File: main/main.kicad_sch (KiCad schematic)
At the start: 8 parts, among them J1 USB_C_Receptacle_USB2.0, U1 ATmega32U4-A, Y1 16MHz

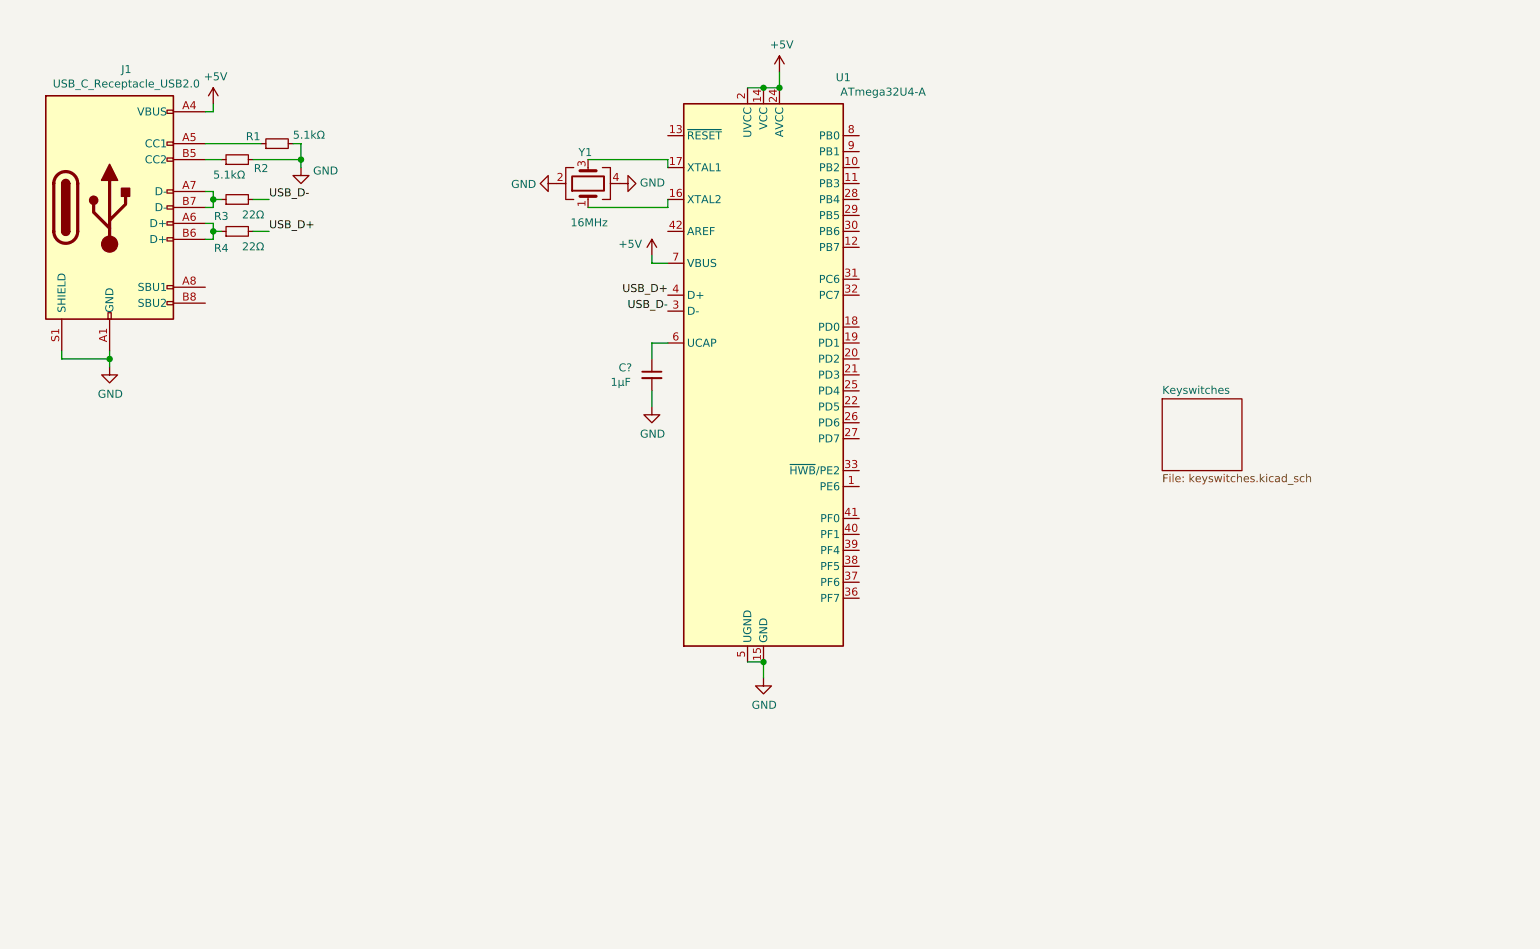
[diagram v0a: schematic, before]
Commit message: Add proposed layout, start LEDs
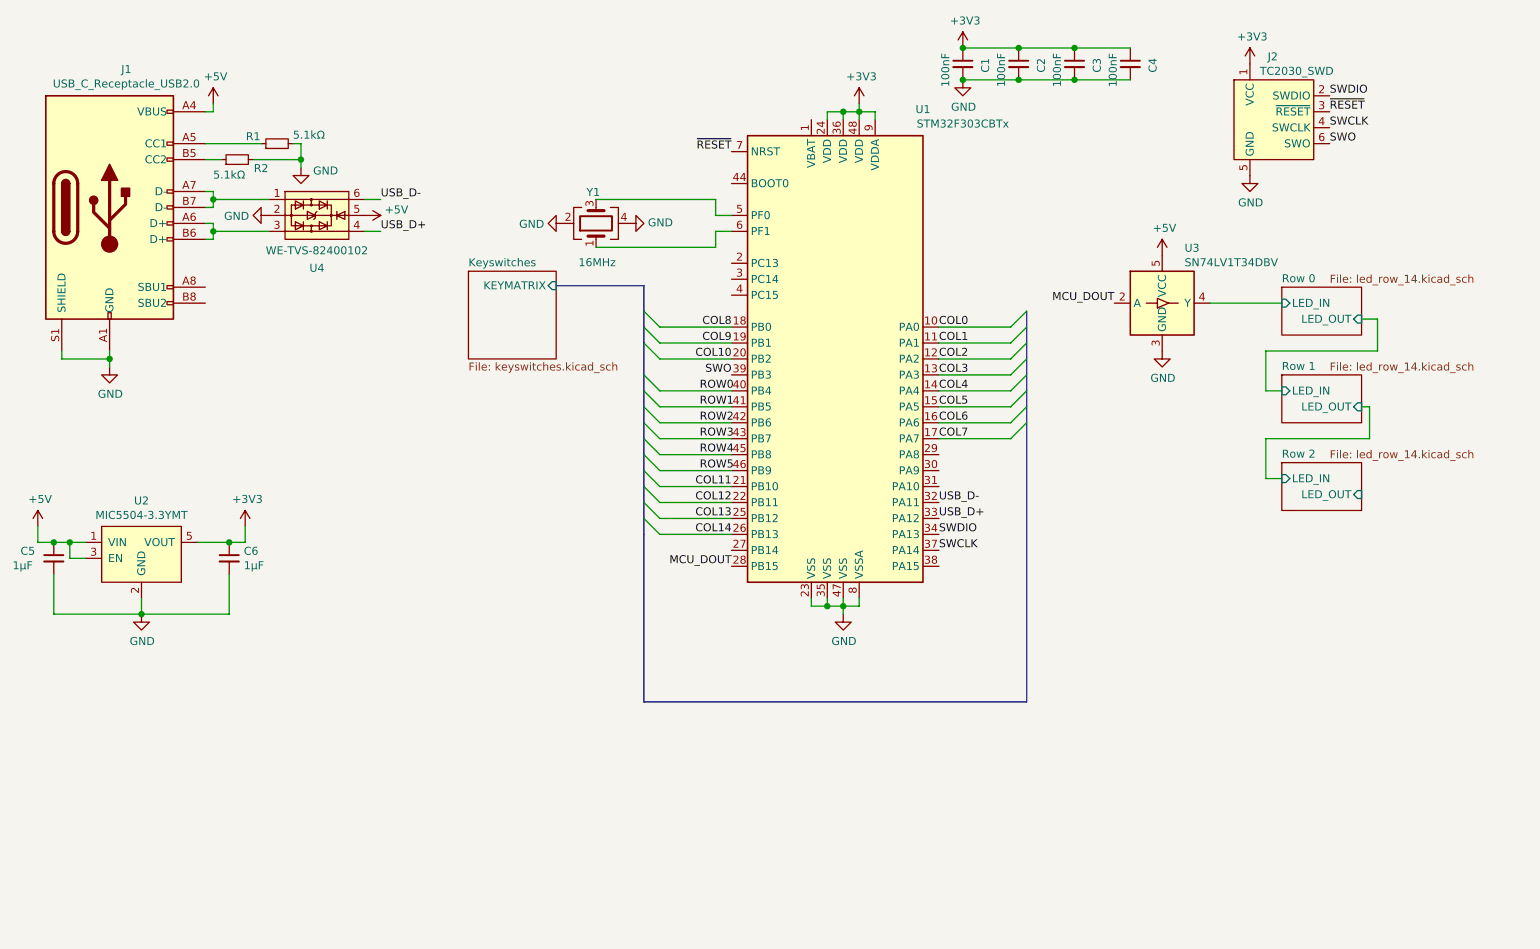
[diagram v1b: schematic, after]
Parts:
- removed C?: 1µF, symbol Device:C_Small
- removed R3, R4: 22Ω, symbol Device:R_Small
- removed U1: ATmega32U4-A, Package_QFP:TQFP-44_10x10mm_P0.8mm, symbol MCU_Microchip_ATmega:ATmega32U4-A
- added C1, C2, C3, C4: 100nF, symbol Device:C_Small
- added C5, C6: 1µF, symbol Device:C_Small
- added J2: TC2030_SWD, Connector:Tag-Connect_TC2030-IDC-NL_2x03_P1.27mm_Vertical, symbol chonc60:TC2030_SWD
- added U1: STM32F303CBTx, Package_QFP:LQFP-48_7x7mm_P0.5mm, symbol MCU_ST_STM32F3:STM32F303CBTx
- added U2: MIC5504-3.3YMT, Package_TO_SOT_SMD:SOT-23-5, symbol chonc60:MIC550x
- added U3: SN74LV1T34DBV, Package_TO_SOT_SMD:SOT-23-5, symbol Logic_LevelTranslator:SN74LV1T34DBV
- added U4: WE-TVS-82400102, Package_TO_SOT_SMD:SOT-23-6, symbol Power_Protection:WE-TVS-82400102
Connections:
- net +5V: now also C5.1, U2.1 (VIN), U2.3 (EN), U3.5 (VCC), U4.5
- net GND: now also C1.2, C2.2, C3.2, C4.2, C5.2, C6.2, J2.5 (GND), U1.23 (VSS), U1.35 (VSS), U1.47 (VSS), U1.8 (VSSA), U2.2 (GND), U3.3 (GND), U4.2
- net USB_D+: now also U1.33 (PA12), U4.4
- net USB_D-: now also U1.32 (PA11), U4.6
- net at J1.A6 (D+), J1.B6 (D+): now also U4.3
- net at J1.A7 (D-), J1.B7 (D-): now also U4.1
- net at Y1.1: now also U1.6 (PF1)
- net at Y1.3: now also U1.5 (PF0)
- new net +3V3: C1.1, C2.1, C3.1, C4.1, C6.1, J2.1 (VCC), U1.24 (VDD), U1.36 (VDD), U1.48 (VDD), U1.9 (VDDA), U2.5 (VOUT)
- new net COL0: U1.10 (PA0)
- new net COL1: U1.11 (PA1)
- new net COL10: U1.20 (PB2)
- new net COL11: U1.21 (PB10)
- new net COL12: U1.22 (PB11)
- new net COL13: U1.25 (PB12)
- new net COL14: U1.26 (PB13)
- new net COL2: U1.12 (PA2)
- new net COL3: U1.13 (PA3)
- new net COL4: U1.14 (PA4)
- new net COL5: U1.15 (PA5)
- new net COL6: U1.16 (PA6)
- new net COL7: U1.17 (PA7)
- new net COL8: U1.18 (PB0)
- new net COL9: U1.19 (PB1)
- new net MCU_DOUT: U1.28 (PB15), U3.2 (A)
- new net ROW0: U1.40 (PB4)
- new net ROW1: U1.41 (PB5)
- new net ROW2: U1.42 (PB6)
- new net ROW3: U1.43 (PB7)
- new net ROW4: U1.45 (PB8)
- new net ROW5: U1.46 (PB9)
- new net Row 0/LED_IN: U3.4 (Y)
- new net SWCLK: J2.4 (SWCLK), U1.37 (PA14)
- new net SWDIO: J2.2 (SWDIO), U1.34 (PA13)
- new net SWO: J2.6 (SWO), U1.39 (PB3)
- new net ~RESET: J2.3 (~RESET), U1.7 (NRST)
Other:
- added sheet Row 0 (led_row_14.kicad_sch)
- added sheet Row 1 (led_row_14.kicad_sch)
- added sheet Row 2 (led_row_14.kicad_sch)
- sheet Keyswitches ports: added KEYMATRIX; removed none
- moved on the sheet: Y1

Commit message: Initial schematic complete
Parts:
- renumbered U3 to U2, U4 to U3, U2 to U4
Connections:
- no-connect marks 0 -> 9
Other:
- added sheet Row 3 (led_row_13.kicad_sch)
- added sheet Row 4 (led_row_12.kicad_sch)
- added sheet Row 5 (led_row_10.kicad_sch)
- sheet Row 0: file led_row_14.kicad_sch -> led_row_15.kicad_sch

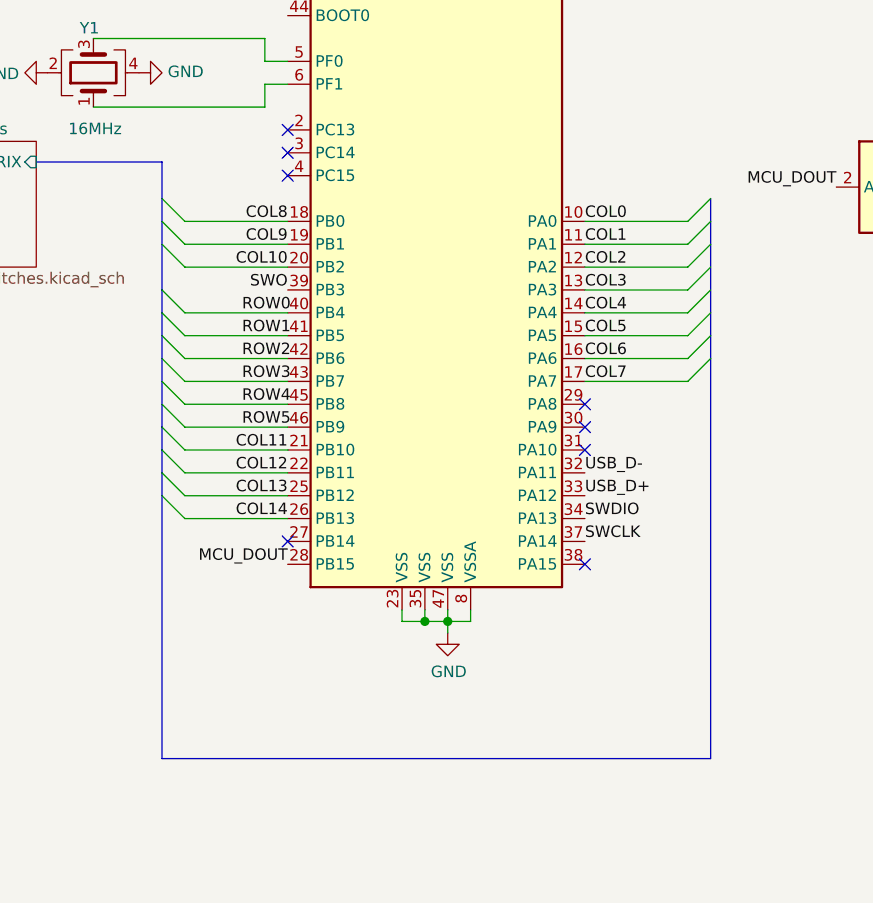
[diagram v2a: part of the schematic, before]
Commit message: Start placing components
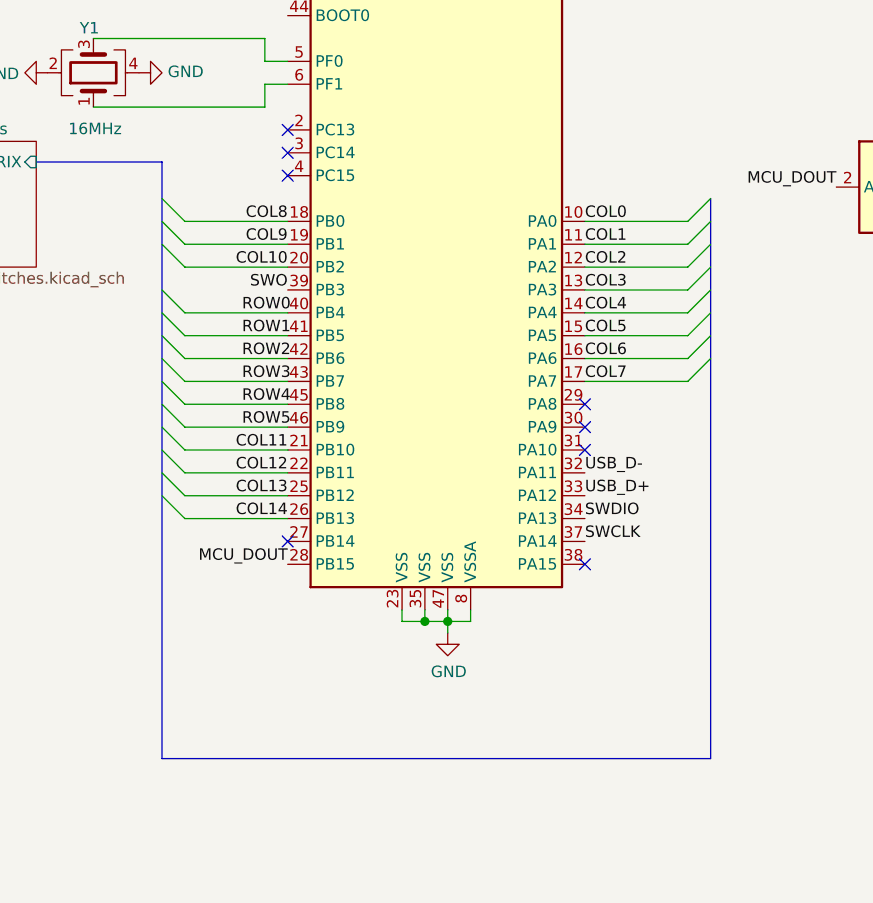
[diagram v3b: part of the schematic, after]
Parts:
- C1, C2, C3, C4, C5, C6: footprint (none) -> Capacitor_SMD:C_0603_1608Metric
- J1: footprint (none) -> chonc60:USB_C_Receptacle_JING_C167321
- R1, R2: footprint (none) -> Resistor_SMD:R_0603_1608Metric

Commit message: Start placing diodes
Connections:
- no-connect marks 9 -> 12
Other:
- sheet Keyswitches ports: added COL[0..14], ROW[0..5]; removed KEYMATRIX

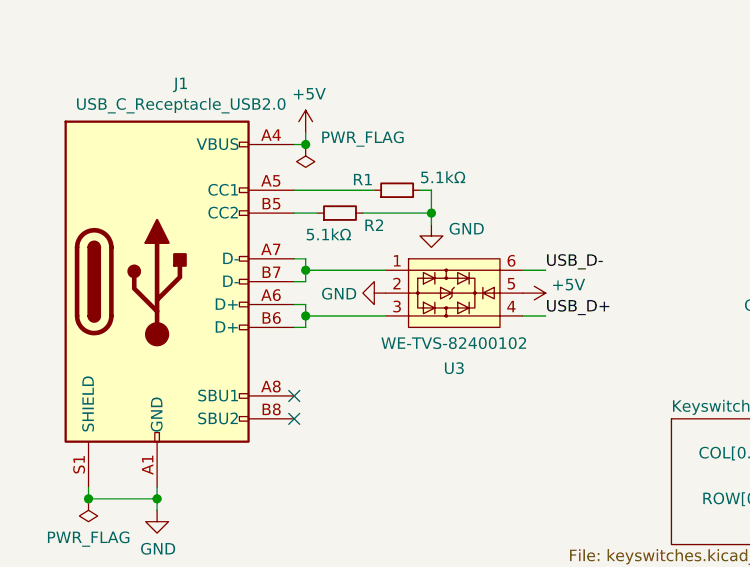
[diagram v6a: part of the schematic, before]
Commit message: Make LEDs make more sense, with automation!
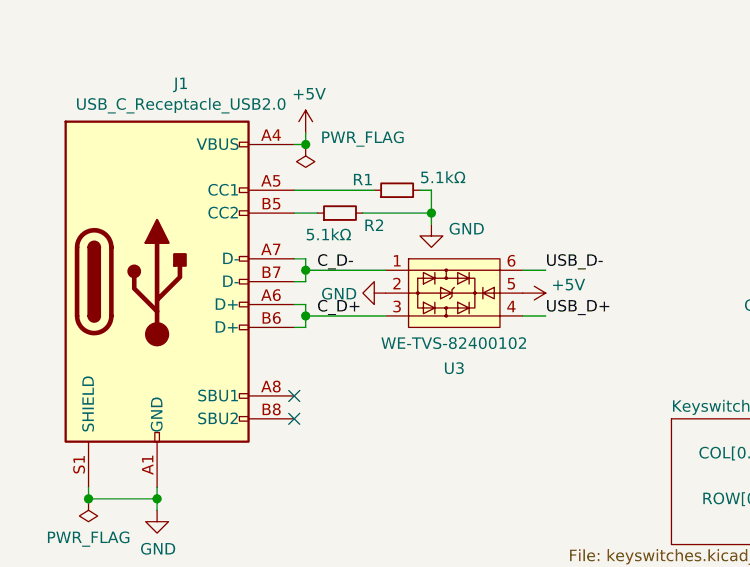
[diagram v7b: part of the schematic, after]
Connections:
- net C_D+: now reaches J1.A6 (D+), J1.B6 (D+), U3.3
- net C_D-: now reaches J1.A7 (D-), J1.B7 (D-), U3.1
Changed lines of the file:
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@@
     (stroke (width 0) (type solid) (color 0 0 0 0))
+  )
+  (label "C_D-" (at 53.34 46.99 0)
+    (effects (font (size 1.27 1.27)) (justify left bottom))
+  )
+  (label "C_D+" (at 53.34 52.07 0)
+    (effects (font (size 1.27 1.27)) (justify left bottom))
   )
   (label "USB_D-" (at 78.74 46.99 0)

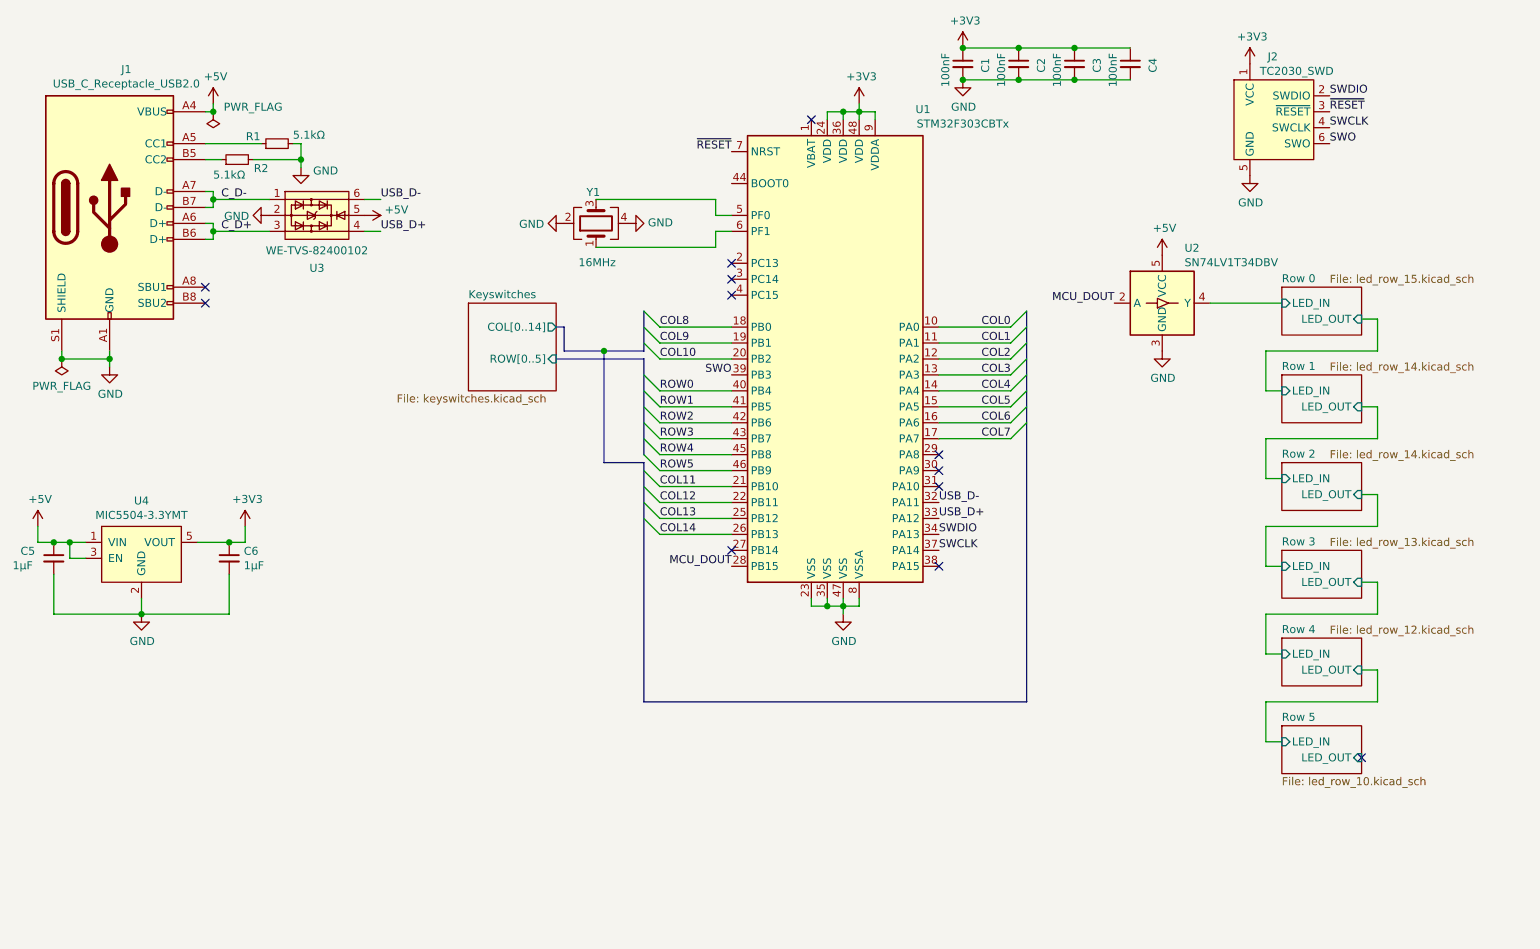
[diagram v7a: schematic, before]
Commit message: Update to new keyboard layout
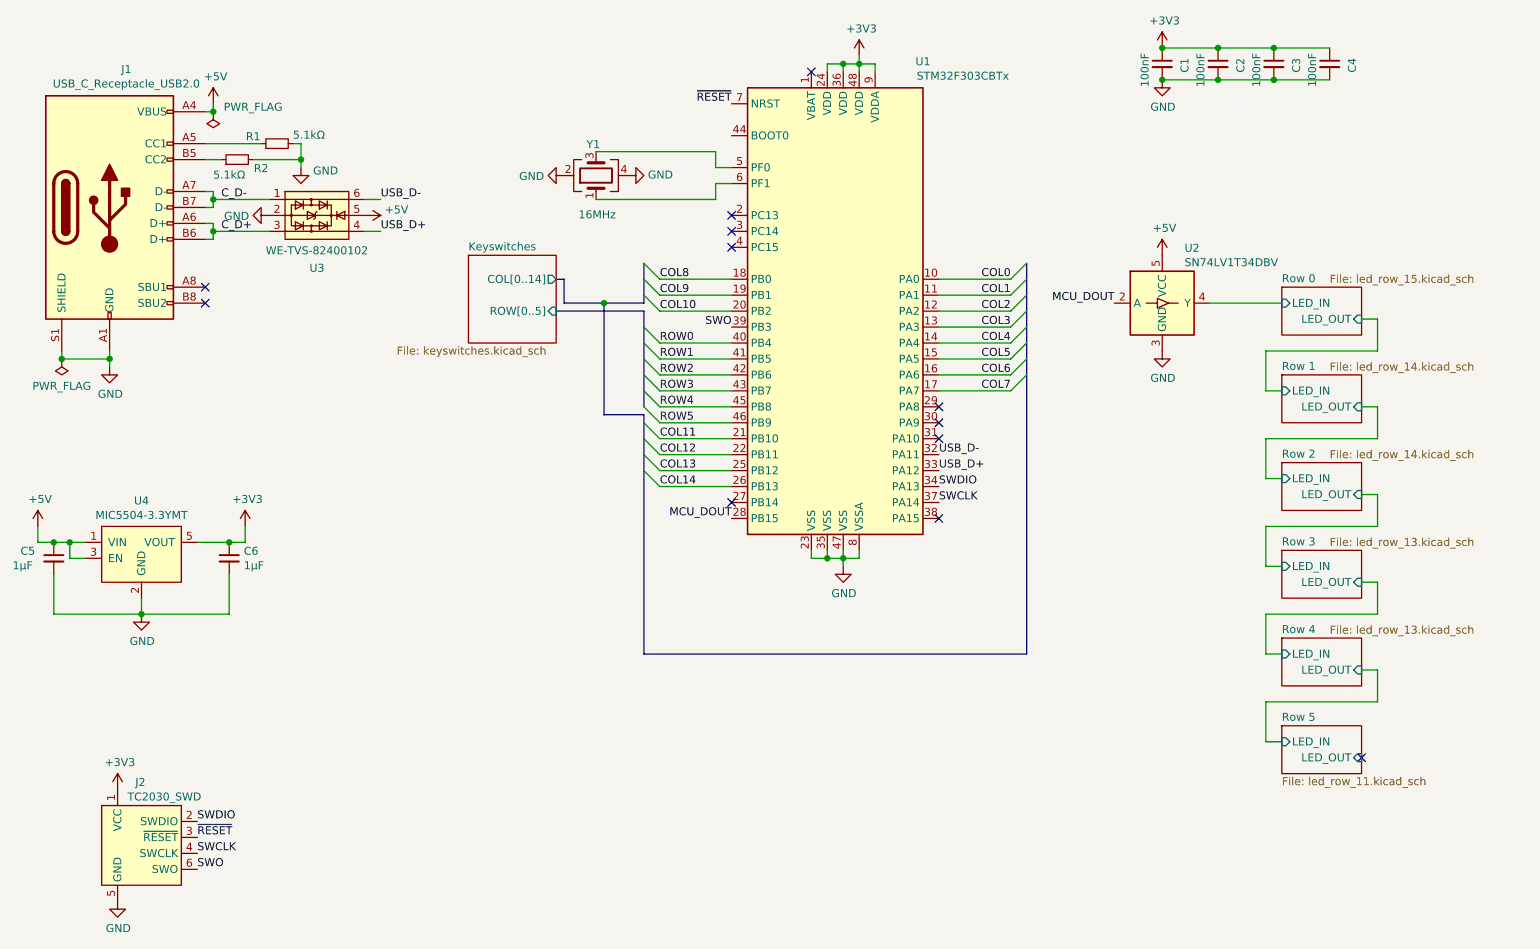
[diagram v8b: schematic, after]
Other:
- sheet Row 4: file led_row_12.kicad_sch -> led_row_13.kicad_sch
- sheet Row 5: file led_row_10.kicad_sch -> led_row_11.kicad_sch
- moved on the sheet: C1, C2, C3, C4, J2, U1, Y1
